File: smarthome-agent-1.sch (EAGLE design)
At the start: 4 parts, among them U1 ATMEGA328P_PDIP_EZ

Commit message: Add new elements
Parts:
- added IC2: 7808T, linear:7808T
- added Q1: 16Mhz, special:XTAL/S
- C1, C2: value (none) -> 100nF
- R1: value 10k Ohm -> 10kOhm
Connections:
- removed net N$2: C1.1, U1.VCC
- removed net N$3: C2.1, U1.AVCC
- new net N$5: Q1.2, U1.PB7(XTAL2/TOSC2)
- new net N$6: Q1.1, U1.PB6(XTAL1/TOSC1)
- net AGND: now also IC2.GND
- net VCC: now also C1.1, C2.1, IC2.VI, U1.AVCC, U1.VCC
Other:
- moved on the sheet: C2
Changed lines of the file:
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@@
 <part name="P+1" library="supply1" library_urn="urn:adsk.eagle:library:371" deviceset="VCC" device=""/>
 <part name="AGND1" library="supply1" library_urn="urn:adsk.eagle:library:371" deviceset="AGND" device=""/>
-<part name="R1" library="rcl" library_urn="urn:adsk.eagle:library:334" deviceset="R-EU_" device="0204/7" package3d_urn="urn:adsk.eagle:package:23498/1" value="10k Ohm"/>
-<part name="C1" library="rcl" library_urn="urn:adsk.eagle:library:334" deviceset="C-EU" device="025-024X044" package3d_urn="urn:adsk.eagle:package:23630/1"/>
-<part name="C2" library="rcl" library_urn="urn:adsk.eagle:library:334" deviceset="C-EU" device="025-024X044" package3d_urn="urn:adsk.eagle:package:23630/1"/>
+<part name="R1" library="rcl" library_urn="urn:adsk.eagle:library:334" deviceset="R-EU_" device="0204/7" package3d_urn="urn:adsk.eagle:package:23498/1" value="10kOhm"/>
+<part name="C1" library="rcl" library_urn="urn:adsk.eagle:library:334" deviceset="C-EU" device="025-024X044" package3d_urn="urn:adsk.eagle:package:23630/1" value="100nF"/>
+<part name="C2" library="rcl" library_urn="urn:adsk.eagle:library:334" deviceset="C-EU" device="025-024X044" package3d_urn="urn:adsk.eagle:package:23630/1" value="100nF"/>
+<part name="Q1" library="special" library_urn="urn:adsk.eagle:library:367" deviceset="XTAL/S" device="" package3d_urn="urn:adsk.eagle:package:26647/2" value="16Mhz"/>
+<part name="IC2" library="linear" library_urn="urn:adsk.eagle:library:262" deviceset="78*" device="T" package3d_urn="urn:adsk.eagle:package:16414/1" technology="08"/>
 </parts>
 <sheets>
@@
 <instance part="R1" gate="G$1" x="124.46" y="96.52"/>
 <instance part="C1" gate="G$1" x="124.46" y="86.36"/>
-<instance part="C2" gate="G$1" x="116.84" y="88.9"/>
+<instance part="C2" gate="G$1" x="111.76" y="88.9"/>
+<instance part="Q1" gate="G$1" x="116.84" y="68.58"/>
+<instance part="IC2" gate="A1" x="81.28" y="83.82"/>
 </instances>
 <busses>
@@
 <wire x1="134.62" y1="25.4" x2="134.62" y2="38.1" width="0.1524" layer="91"/>
 <pinref part="C1" gate="G$1" pin="2"/>
-<wire x1="124.46" y1="81.28" x2="124.46" y2="38.1" width="0.1524" layer="91"/>
+<wire x1="124.46" y1="81.28" x2="124.46" y2="78.74" width="0.1524" layer="91"/>
+<wire x1="124.46" y1="78.74" x2="124.46" y2="38.1" width="0.1524" layer="91"/>
 <wire x1="124.46" y1="38.1" x2="134.62" y2="38.1" width="0.1524" layer="91"/>
 <junction x="134.62" y="38.1"/>
 <pinref part="C2" gate="G$1" pin="2"/>
-<wire x1="116.84" y1="83.82" x2="116.84" y2="81.28" width="0.1524" layer="91"/>
-<wire x1="116.84" y1="81.28" x2="124.46" y2="81.28" width="0.1524" layer="91"/>
-<junction x="124.46" y="81.28"/>
+<wire x1="111.76" y1="83.82" x2="111.76" y2="78.74" width="0.1524" layer="91"/>
+<wire x1="111.76" y1="78.74" x2="124.46" y2="78.74" width="0.1524" layer="91"/>
+<junction x="124.46" y="78.74"/>
+<pinref part="IC2" gate="A1" pin="GND"/>
+<wire x1="81.28" y1="76.2" x2="81.28" y2="25.4" width="0.1524" layer="91"/>
+<wire x1="81.28" y1="25.4" x2="96.52" y2="25.4" width="0.1524" layer="91"/>
+<junction x="96.52" y="25.4"/>
 </segment>
 </net>
@@
 <pinref part="R1" gate="G$1" pin="1"/>
 <wire x1="91.44" y1="104.14" x2="91.44" y2="96.52" width="0.1524" layer="91"/>
-<wire x1="91.44" y1="96.52" x2="119.38" y2="96.52" width="0.1524" layer="91"/>
-</segment>
-</net>
-<net name="N$2" class="0">
-<segment>
+<wire x1="91.44" y1="96.52" x2="111.76" y2="96.52" width="0.1524" layer="91"/>
+<pinref part="C2" gate="G$1" pin="1"/>
+<pinref part="U1" gate="U1" pin="AVCC"/>
+<wire x1="111.76" y1="96.52" x2="119.38" y2="96.52" width="0.1524" layer="91"/>
+<wire x1="111.76" y1="91.44" x2="124.46" y2="91.44" width="0.1524" layer="91"/>
+<wire x1="124.46" y1="91.44" x2="134.62" y2="91.44" width="0.1524" layer="91"/>
+<wire x1="111.76" y1="91.44" x2="111.76" y2="96.52" width="0.1524" layer="91"/>
+<junction x="111.76" y="91.44"/>
+<junction x="111.76" y="96.52"/>
 <pinref part="C1" gate="G$1" pin="1"/>
 <pinref part="U1" gate="U1" pin="VCC"/>
 <wire x1="124.46" y1="88.9" x2="134.62" y2="88.9" width="0.1524" layer="91"/>
+<wire x1="124.46" y1="88.9" x2="124.46" y2="91.44" width="0.1524" layer="91"/>
+<junction x="124.46" y="88.9"/>
+<junction x="124.46" y="91.44"/>
+<pinref part="IC2" gate="A1" pin="VI"/>
+<wire x1="71.12" y1="83.82" x2="63.5" y2="83.82" width="0.1524" layer="91"/>
+<wire x1="63.5" y1="83.82" x2="63.5" y2="96.52" width="0.1524" layer="91"/>
+<wire x1="63.5" y1="96.52" x2="91.44" y2="96.52" width="0.1524" layer="91"/>
+<junction x="91.44" y="96.52"/>
 </segment>
 </net>
-<net name="N$3" class="0">
+<net name="N$5" class="0">
 <segment>
-<pinref part="C2" gate="G$1" pin="1"/>
-<pinref part="U1" gate="U1" pin="AVCC"/>
-<wire x1="116.84" y1="91.44" x2="134.62" y2="91.44" width="0.1524" layer="91"/>
+<pinref part="Q1" gate="G$1" pin="2"/>
+<pinref part="U1" gate="U1" pin="PB7(XTAL2/TOSC2)"/>
+<wire x1="121.92" y1="68.58" x2="121.92" y2="66.04" width="0.1524" layer="91"/>
+<wire x1="121.92" y1="66.04" x2="134.62" y2="66.04" width="0.1524" layer="91"/>
 </segment>
 </net>
+<net name="N$6" class="0">
+<segment>
+<pinref part="Q1" gate="G$1" pin="1"/>
+<pinref part="U1" gate="U1" pin="PB6(XTAL1/TOSC1)"/>
+<wire x1="111.76" y1="68.58" x2="111.76" y2="71.12" width="0.1524" layer="91"/>
+<wire x1="111.76" y1="71.12" x2="134.62" y2="71.12" width="0.1524" layer="91"/>
+</segment>
+</net>

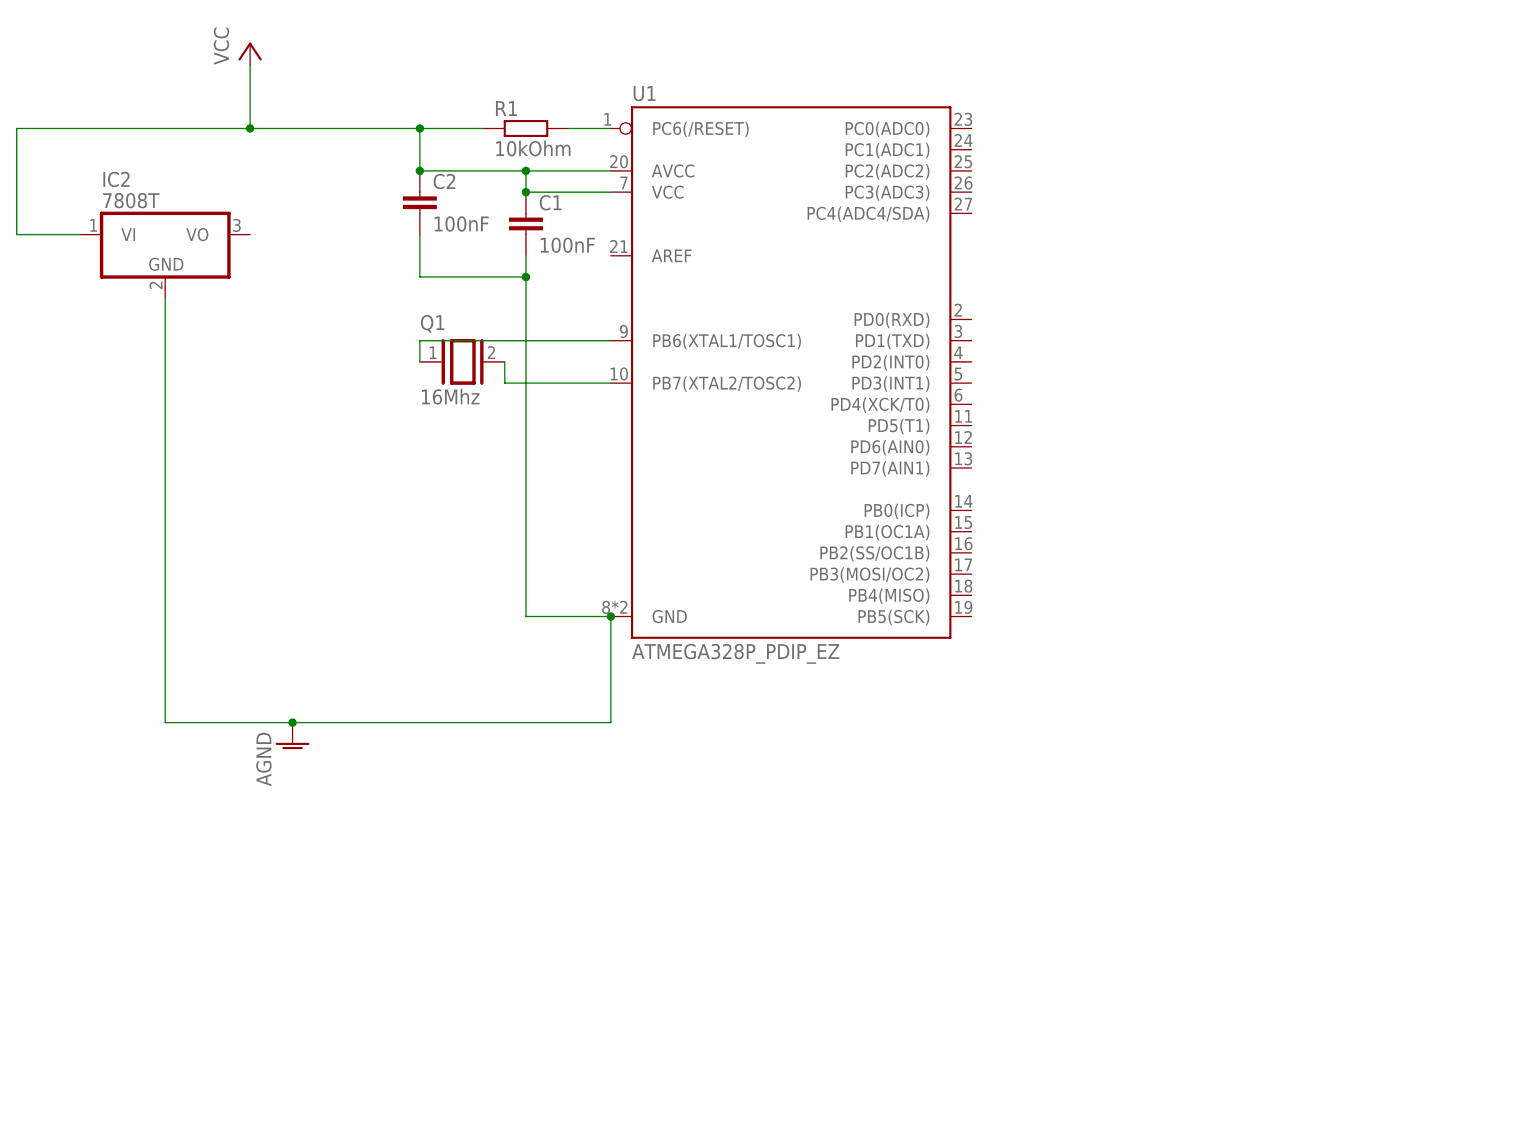
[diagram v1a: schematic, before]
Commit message: Add ESP01
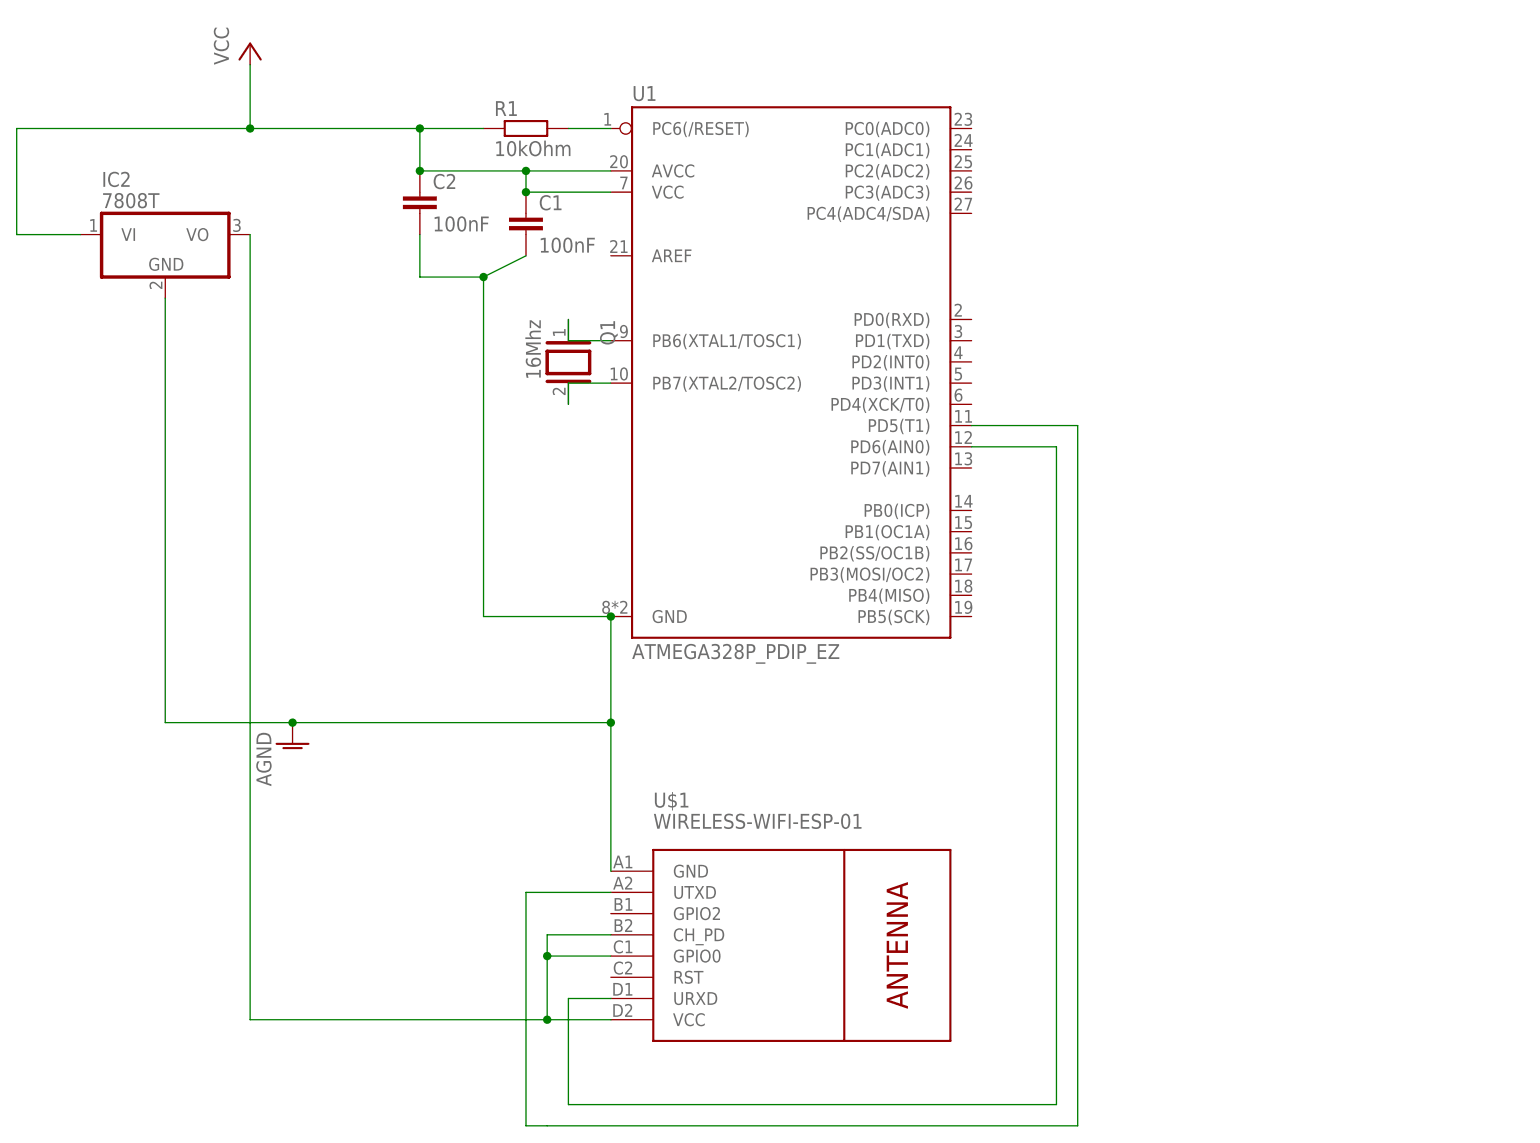
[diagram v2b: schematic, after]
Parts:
- added U$1: WIRELESS-WIFI-ESP-01, diy-modules:WIRELESS-WIFI-ESP-01
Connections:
- new net N$2: IC2.VO, U$1.CH_PD, U$1.GPIO0, U$1.VCC
- new net N$5: U$1.UTXD, U1.PD5(T1)
- new net N$6: U$1.URXD, U1.PD6(AIN0)
- net AGND: now also U$1.GND
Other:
- moved on the sheet: Q1
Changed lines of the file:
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@@
 <part name="Q1" library="special" library_urn="urn:adsk.eagle:library:367" deviceset="XTAL/S" device="" package3d_urn="urn:adsk.eagle:package:26647/2" value="16Mhz"/>
 <part name="IC2" library="linear" library_urn="urn:adsk.eagle:library:262" deviceset="78*" device="T" package3d_urn="urn:adsk.eagle:package:16414/1" technology="08"/>
+<part name="U$1" library="diy-modules" deviceset="WIRELESS-WIFI-ESP-01" device=""/>
 </parts>
 <sheets>
@@
 <instance part="C1" gate="G$1" x="124.46" y="86.36"/>
 <instance part="C2" gate="G$1" x="111.76" y="88.9"/>
-<instance part="Q1" gate="G$1" x="116.84" y="68.58"/>
+<instance part="Q1" gate="G$1" x="129.54" y="68.58" rot="R270"/>
 <instance part="IC2" gate="A1" x="81.28" y="83.82"/>
+<instance part="U$1" gate="G$1" x="157.48" y="-2.54"/>
 </instances>
 <busses>
@@
 <wire x1="134.62" y1="25.4" x2="134.62" y2="38.1" width="0.1524" layer="91"/>
 <pinref part="C1" gate="G$1" pin="2"/>
-<wire x1="124.46" y1="81.28" x2="124.46" y2="78.74" width="0.1524" layer="91"/>
-<wire x1="124.46" y1="78.74" x2="124.46" y2="38.1" width="0.1524" layer="91"/>
-<wire x1="124.46" y1="38.1" x2="134.62" y2="38.1" width="0.1524" layer="91"/>
+<wire x1="124.46" y1="81.28" x2="119.38" y2="78.74" width="0.1524" layer="91"/>
+<wire x1="119.38" y1="78.74" x2="119.38" y2="38.1" width="0.1524" layer="91"/>
+<wire x1="119.38" y1="38.1" x2="134.62" y2="38.1" width="0.1524" layer="91"/>
 <junction x="134.62" y="38.1"/>
 <pinref part="C2" gate="G$1" pin="2"/>
 <wire x1="111.76" y1="83.82" x2="111.76" y2="78.74" width="0.1524" layer="91"/>
-<wire x1="111.76" y1="78.74" x2="124.46" y2="78.74" width="0.1524" layer="91"/>
-<junction x="124.46" y="78.74"/>
+<wire x1="111.76" y1="78.74" x2="119.38" y2="78.74" width="0.1524" layer="91"/>
+<junction x="119.38" y="78.74"/>
 <pinref part="IC2" gate="A1" pin="GND"/>
 <wire x1="81.28" y1="76.2" x2="81.28" y2="25.4" width="0.1524" layer="91"/>
 <wire x1="81.28" y1="25.4" x2="96.52" y2="25.4" width="0.1524" layer="91"/>
 <junction x="96.52" y="25.4"/>
+<pinref part="U$1" gate="G$1" pin="GND"/>
+<wire x1="134.62" y1="7.62" x2="134.62" y2="25.4" width="0.1524" layer="91"/>
+<junction x="134.62" y="25.4"/>
 </segment>
 </net>
@@
 </segment>
 </net>
-<net name="N$5" class="0">
+<net name="N$2" class="0">
+<segment>
+<pinref part="IC2" gate="A1" pin="VO"/>
+<pinref part="U$1" gate="G$1" pin="VCC"/>
+<wire x1="91.44" y1="83.82" x2="91.44" y2="-10.16" width="0.1524" layer="91"/>
+<wire x1="91.44" y1="-10.16" x2="127" y2="-10.16" width="0.1524" layer="91"/>
+<pinref part="U$1" gate="G$1" pin="GPIO0"/>
+<wire x1="127" y1="-10.16" x2="134.62" y2="-10.16" width="0.1524" layer="91"/>
+<wire x1="134.62" y1="-2.54" x2="127" y2="-2.54" width="0.1524" layer="91"/>
+<wire x1="127" y1="-2.54" x2="127" y2="-10.16" width="0.1524" layer="91"/>
+<junction x="127" y="-10.16"/>
+<pinref part="U$1" gate="G$1" pin="CH_PD"/>
+<wire x1="134.62" y1="0" x2="127" y2="0" width="0.1524" layer="91"/>
+<wire x1="127" y1="0" x2="127" y2="-2.54" width="0.1524" layer="91"/>
+<junction x="127" y="-2.54"/>
+</segment>
+</net>
+<net name="N$3" class="0">
+<segment>
+<pinref part="Q1" gate="G$1" pin="1"/>
+<pinref part="U1" gate="U1" pin="PB6(XTAL1/TOSC1)"/>
+<wire x1="129.54" y1="73.66" x2="129.54" y2="71.12" width="0.1524" layer="91"/>
+<wire x1="129.54" y1="71.12" x2="134.62" y2="71.12" width="0.1524" layer="91"/>
+</segment>
+</net>
+<net name="N$4" class="0">
 <segment>
 <pinref part="Q1" gate="G$1" pin="2"/>
 <pinref part="U1" gate="U1" pin="PB7(XTAL2/TOSC2)"/>
-<wire x1="121.92" y1="68.58" x2="121.92" y2="66.04" width="0.1524" layer="91"/>
-<wire x1="121.92" y1="66.04" x2="134.62" y2="66.04" width="0.1524" layer="91"/>
+<wire x1="129.54" y1="63.5" x2="129.54" y2="66.04" width="0.1524" layer="91"/>
+<wire x1="129.54" y1="66.04" x2="134.62" y2="66.04" width="0.1524" layer="91"/>
+</segment>
+</net>
+<net name="N$5" class="0">
+<segment>
+<wire x1="190.5" y1="-22.86" x2="190.5" y2="60.96" width="0.1524" layer="91"/>
+<pinref part="U1" gate="U1" pin="PD5(T1)"/>
+<wire x1="190.5" y1="60.96" x2="177.8" y2="60.96" width="0.1524" layer="91"/>
+<wire x1="190.5" y1="-22.86" x2="127" y2="-22.86" width="0.1524" layer="91"/>
+<wire x1="127" y1="-22.86" x2="124.46" y2="-22.86" width="0.1524" layer="91"/>
+<wire x1="124.46" y1="-22.86" x2="124.46" y2="5.08" width="0.1524" layer="91"/>
+<pinref part="U$1" gate="G$1" pin="UTXD"/>
+<wire x1="124.46" y1="5.08" x2="134.62" y2="5.08" width="0.1524" layer="91"/>
 </segment>
 </net>
 <net name="N$6" class="0">
 <segment>
-<pinref part="Q1" gate="G$1" pin="1"/>
-<pinref part="U1" gate="U1" pin="PB6(XTAL1/TOSC1)"/>
-<wire x1="111.76" y1="68.58" x2="111.76" y2="71.12" width="0.1524" layer="91"/>
-<wire x1="111.76" y1="71.12" x2="134.62" y2="71.12" width="0.1524" layer="91"/>
+<pinref part="U$1" gate="G$1" pin="URXD"/>
+<wire x1="134.62" y1="-7.62" x2="129.54" y2="-7.62" width="0.1524" layer="91"/>
+<wire x1="129.54" y1="-7.62" x2="129.54" y2="-20.32" width="0.1524" layer="91"/>
+<wire x1="129.54" y1="-20.32" x2="187.96" y2="-20.32" width="0.1524" layer="91"/>
+<pinref part="U1" gate="U1" pin="PD6(AIN0)"/>
+<wire x1="187.96" y1="-20.32" x2="187.96" y2="58.42" width="0.1524" layer="91"/>
+<wire x1="187.96" y1="58.42" x2="177.8" y2="58.42" width="0.1524" layer="91"/>
 </segment>
 </net>

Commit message: Add IDC socket and USB
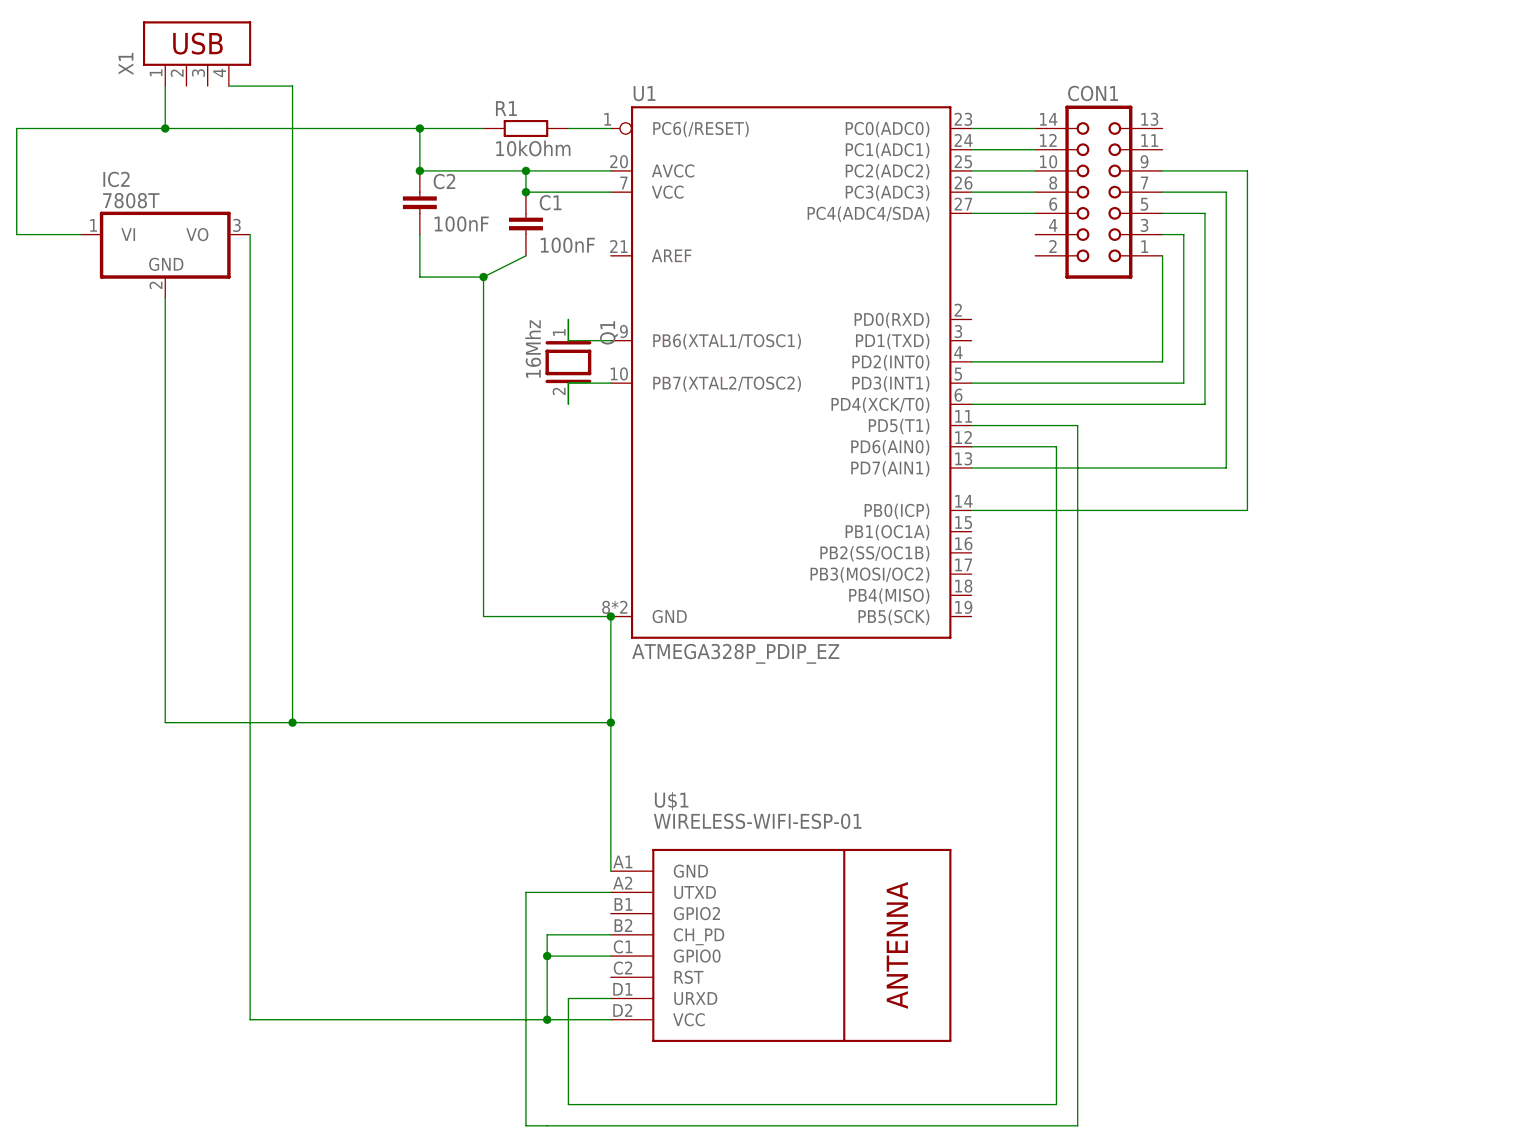
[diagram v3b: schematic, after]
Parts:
- added CON1: (no value), con-harting:CON14
- added X1: (no value), con-amp:USB-787616
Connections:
- removed net AGND: C1.2, C2.2, IC2.GND, U$1.GND, U1.GND
- removed net VCC: C1.1, C2.1, IC2.VI, R1.1, U1.AVCC, U1.VCC
- new net N$10: CON1.7, U1.PD7(AIN1)
- new net N$11: CON1.14, U1.PC0(ADC0)
- new net N$12: CON1.12, U1.PC1(ADC1)
- new net N$13: CON1.10, U1.PC2(ADC2)
- new net N$14: CON1.8, U1.PC3(ADC3)
- new net N$15: CON1.6, U1.PC4(ADC4/SDA)
- new net N$16: CON1.9, U1.PB0(ICP)
- new net N$17: C1.1, C2.1, IC2.VI, R1.1, U1.AVCC, U1.VCC, X1.1
- new net N$18: C1.2, C2.2, IC2.GND, U$1.GND, U1.GND, X1.4
- new net N$7: CON1.1, U1.PD2(INT0)
- new net N$8: CON1.3, U1.PD3(INT1)
- new net N$9: CON1.5, U1.PD4(XCK/T0)
